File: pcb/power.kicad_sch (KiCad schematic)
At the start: 0 parts

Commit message: Completed Initial Power Draft for Review, and Updated Flags
Included notes for review
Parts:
- added C21: 1000pF, Capacitor_SMD:C_0402_1005Metric_Pad0.74x0.62mm_HandSolder, symbol Device:C_Small
- added C22: 0.47uF, Capacitor_SMD:C_0402_1005Metric_Pad0.74x0.62mm_HandSolder, symbol Device:C_Small
- added C23, C34: 1uF, Capacitor_SMD:C_0402_1005Metric_Pad0.74x0.62mm_HandSolder, symbol Device:C_Small
- added C24: 33uF, Capacitor_SMD:C_0402_1005Metric_Pad0.74x0.62mm_HandSolder, symbol Device:C_Small
- added C25: 3300pF, Capacitor_SMD:C_0402_1005Metric_Pad0.74x0.62mm_HandSolder, symbol Device:C_Small
- added C26, C28, C29, C31, C32: 0.1uF, Capacitor_SMD:C_0402_1005Metric_Pad0.74x0.62mm_HandSolder, symbol Device:C_Small
- added C27: 100uF, Capacitor_SMD:C_0402_1005Metric_Pad0.74x0.62mm_HandSolder, symbol Device:C_Small
- added C30, C33, C35, C36: 10uF, Capacitor_SMD:C_0402_1005Metric_Pad0.74x0.62mm_HandSolder, symbol Device:C_Small
- added D1: 5V, Diode_SMD:D_SOD-882, symbol Device:D_TVS_Small
- added L1: 15uH, symbol Device:L_Small
- added L2, L3: 8.2uH, symbol Device:L_Small
- added Q7: Vishay Si7465, symbol Simulation_SPICE:PMOS
- added R13: 0.01Ω, symbol Device:R_Small_US
- added R14: 2.1kΩ, symbol Device:R_Small_US
- added R15: 90.9kΩ, symbol Device:R_Small_US
- added R16: 66.5kΩ, symbol Device:R_Small_US
- added R17, R23: 10kΩ, symbol Device:R_Small_US
- added R18: 3.4kΩ, symbol Device:R_Small_US
- added R19, R21: 69.8kΩ, symbol Device:R_Small_US
- added R20, R22: 22.1kΩ, symbol Device:R_Small_US
- added U3: LM5085, symbol Symbols:LM5085
- added U4: LMR51610, symbol Symbols:LMR51610
- added U5: LMR51606, symbol Symbols:LMR51606
- added U6: LM2775, Package_SON:WSON-8-1EP_2x2mm_P0.5mm_EP0.9x1.6mm_ThermalVias, symbol Regulator_SwitchedCapacitor:LM2775DSG
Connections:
- new net: C25.2, C26.1, R16.2
- new net: C26.2, R17.2, R18.1, U3.3 (FB)
- new net: Q7.1 (D), R13.2, U3.5 (ISEN)
- new net: Q7.2 (G), U3.6 (PGATE)
- new net: D1.2 (A2), L1.1, Q7.3 (S), R16.1
- new net: R23.2, U6.5 (EN)
- new net: C32.1, U5.1 (CB)
- new net: C32.2, L3.1, U5.6 (SW)
- new net: C34.1, U6.3 (C1+)
- new net: C34.2, U6.2 (C1-)
- new net: C28.1, U4.1 (CB)
- new net: C28.2, L2.1, U4.6 (SW)
- new net: C21.2, R14.1, U3.1 (ADJ)
- new net: R15.2, U3.2 (RT)
- new net: R19.2, R20.1, U4.3 (FB)
- new net: R21.2, R22.1, U5.3 (FB)
- new net: C22.2, U3.7 (VCC)
- new net +3V3I: C33.1, L3.2, R21.1, R23.1
- new net +3V3P: C30.1, C36.1, L2.2, R19.1, U6.1 (PFM), U6.4 (OUTDIS), U6.7 (VIN)
- new net +5VCP: C35.1, U6.6 (VOUT)
- new net +5VP: C25.1, C27.1, L1.2, R17.1
- new net +VBAT: C21.1, C22.1, C23.1, C24.1, C29.1, C31.1, R13.1, R14.2, R15.1, U3.8 (VIN), U4.4 (EN), U4.5 (VIN), U5.4 (EN), U5.5 (VIN)
- new net GND: C23.2, C24.2, C27.2, C29.2, C30.2, C31.2, C33.2, C35.2, C36.2, D1.1 (A1), R18.2, R20.2, R22.2, U3.4 (GND), U4.2 (GND), U5.2 (GND), U6.8 (GND), U6.9 (GND)
- no-connect marks 0 -> 7
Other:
- note added: ""CHARGE PUMP""
- note added: "-"
- note added: "16V"
- note added: "3.3V Internal"
- note added: "3.3V Peripheral"
- note added: "5V Peripheral"
- note added: "Charge Pump"
- note added: "DOUBLE CHECK IF I CAN DO THIS"
- note added: "Daughter Board"
- note added: "Internal"
- note added: "Peripheral"
- note added: "Power Overview"
- note added: "Source"
- note added: "{dblquote}BATTERY{dblquote}"
- note added: "{dblquote}MOTOR{dblquote}"

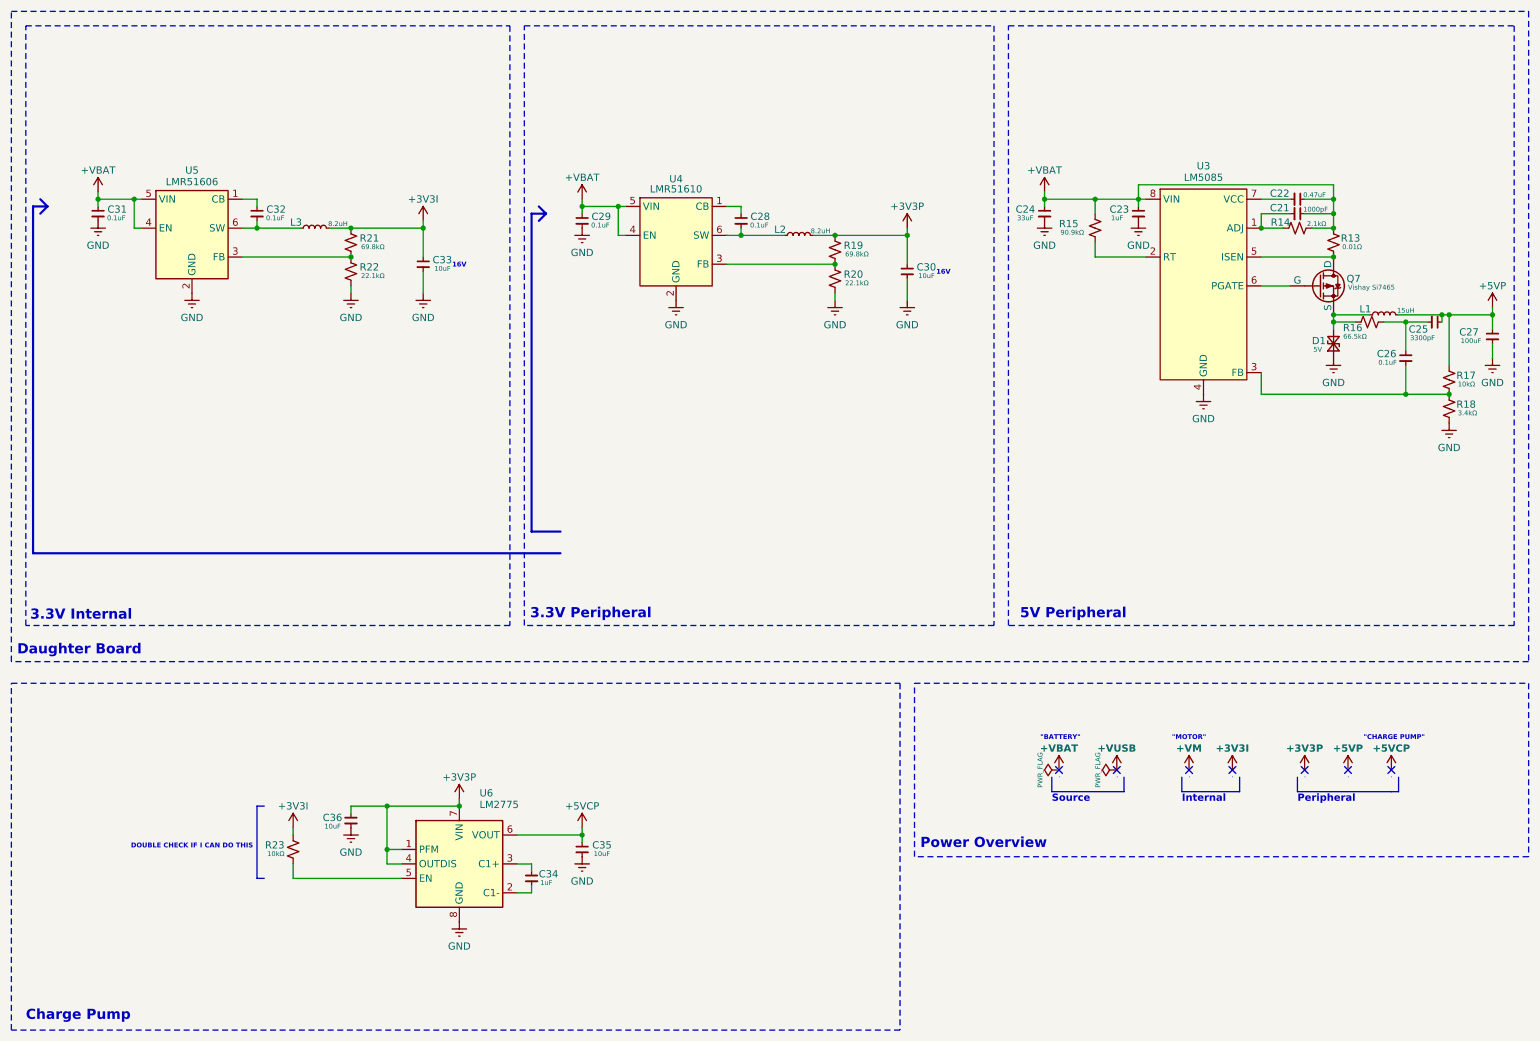
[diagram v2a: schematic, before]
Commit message: Made updates to the power and driver sheet
Fixed converters and added motor connector
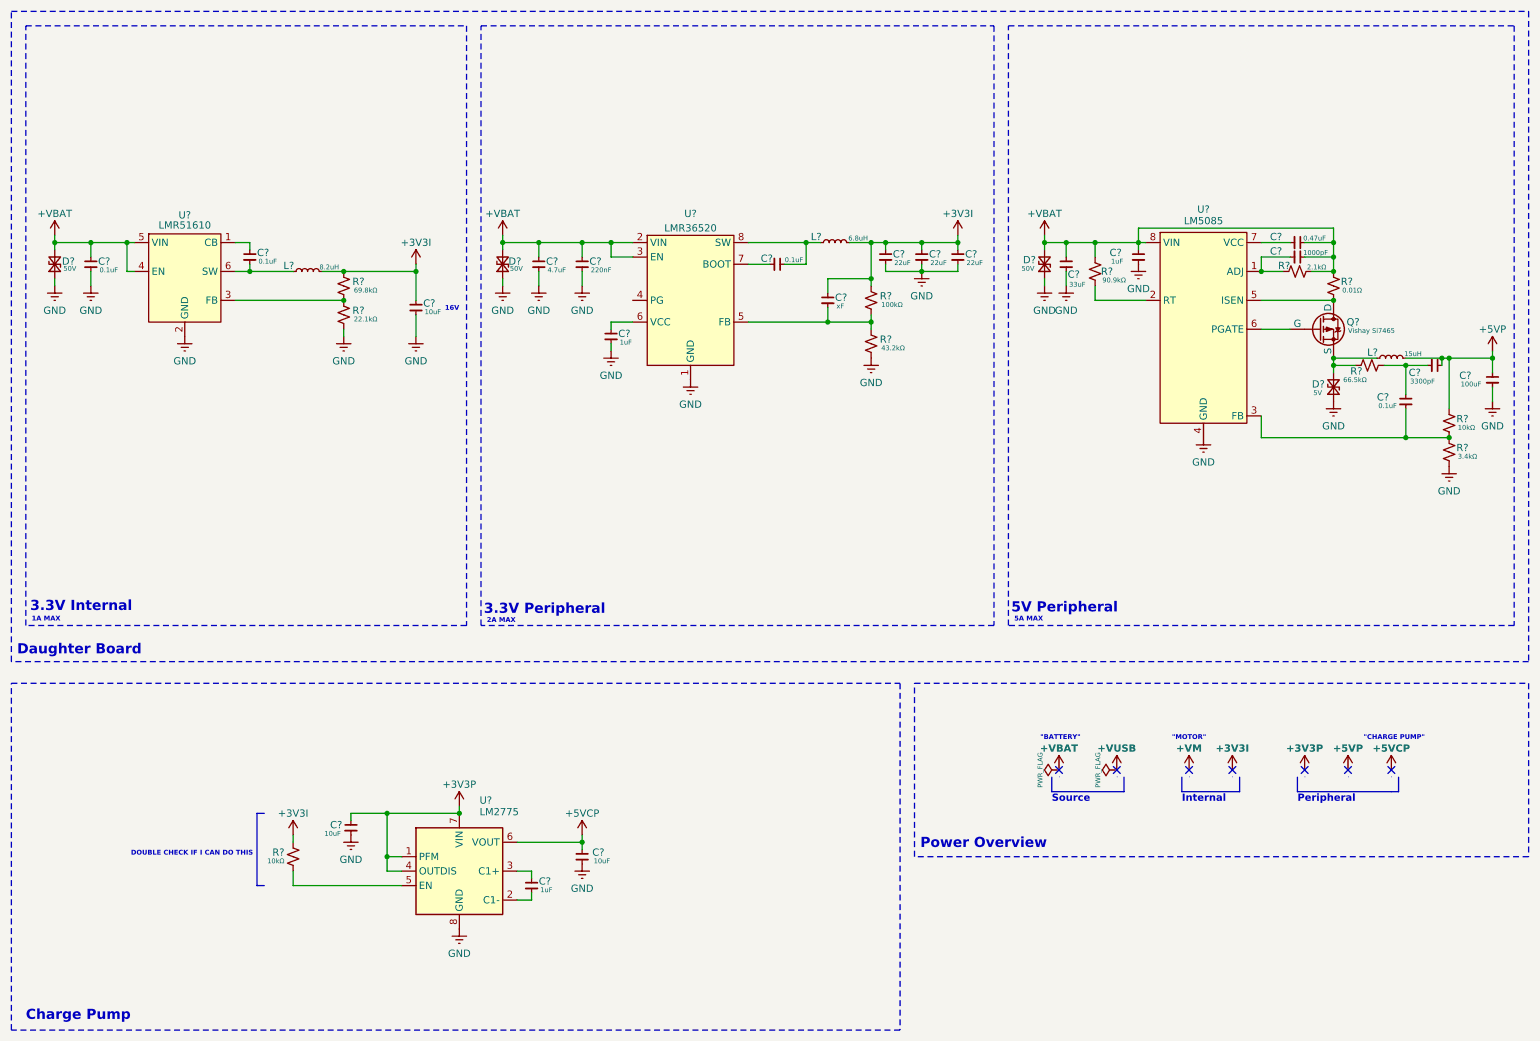
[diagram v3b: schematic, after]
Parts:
- removed C28, C29, C31, C32: 0.1uF, Capacitor_SMD:C_0402_1005Metric_Pad0.74x0.62mm_HandSolder, symbol Device:C_Small
- removed C30, C33: 10uF, Capacitor_SMD:C_0402_1005Metric_Pad0.74x0.62mm_HandSolder, symbol Device:C_Small
- removed L2, L3: 8.2uH, symbol Device:L_Small
- removed R19, R21: 69.8kΩ, symbol Device:R_Small_US
- removed R20, R22: 22.1kΩ, symbol Device:R_Small_US
- removed U4: LMR51610, symbol Symbols:LMR51610
- removed U5: LMR51606, symbol Symbols:LMR51606
- added C? (x3): 22uF, Capacitor_SMD:C_0402_1005Metric_Pad0.74x0.62mm_HandSolder, symbol Device:C_Small
- added C?: 220nF, Capacitor_SMD:C_0402_1005Metric_Pad0.74x0.62mm_HandSolder, symbol Device:C_Small
- added C?: xF, Capacitor_SMD:C_0402_1005Metric_Pad0.74x0.62mm_HandSolder, symbol Device:C_Small
- added C?: 4.7uF, Capacitor_SMD:C_0402_1005Metric_Pad0.74x0.62mm_HandSolder, symbol Device:C_Small
- added C? (x3): 0.1uF, Capacitor_SMD:C_0402_1005Metric_Pad0.74x0.62mm_HandSolder, symbol Device:C_Small
- added C?: 1uF, Capacitor_SMD:C_0402_1005Metric_Pad0.74x0.62mm_HandSolder, symbol Device:C_Small
- added C?: 10uF, Capacitor_SMD:C_0402_1005Metric_Pad0.74x0.62mm_HandSolder, symbol Device:C_Small
- added D? (x3): 50V, symbol Device:D_TVS_Small
- added L?: 8.2uH, symbol Device:L_Small
- added L?: 6.8uH, symbol Device:L_Small
- added R?: 69.8kΩ, symbol Device:R_Small_US
- added R?: 43.2kΩ, symbol Device:R_Small_US
- added R?: 100kΩ, symbol Device:R_Small_US
- added R?: 22.1kΩ, symbol Device:R_Small_US
- added U?: LMR51610, Package_TO_SOT_SMD:SOT-23-6_Handsoldering, symbol Symbols:LMR51610
- added U?: LMR36520, Package_SO:Texas_R-PDSO-G8_EP2.95x4.9mm_Mask2.4x3.1mm_ThermalVias, symbol Symbols:LMR36520
- renumbered C26 to C?, C34 to C?, C23 to C?, C21 to C?, C35 to C?, C25 to C?, C27 to C?, C22 to C?, C24 to C?, C36 to C?, D1 to D?, L1 to L?, Q7 to Q?, R23 to R?, R18 to R?, R16 to R?, R15 to R?, R17 to R?, R14 to R?, R13 to R?, U6 to U?, U3 to U?
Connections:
- net +3V3I: now also C?.1, C?.1, C?.1, C?.1, C?.1, L?.2, L?.2, R?.1, R?.1
- net +VBAT: now also C?.1, C?.1, C?.1, D?.2 (A2), D?.2 (A2), D?.2 (A2), U?.2 (VIN), U?.3 (EN), U?.4 (EN), U?.5 (VIN)
- net GND: now also C?.2, C?.2, C?.2, C?.2, C?.2, C?.2, C?.2, C?.2, D?.1 (A1), D?.1 (A1), D?.1 (A1), R?.2, R?.2, U?.1 (GND), U?.2 (GND), U?.9 (EP)
- new net: C?.2, L?.1, U?.6 (SW)
- new net: C?.1, U?.1 (CB)
- new net: R?.1, R?.2, U?.3 (FB)
- new net: C?.2, R?.1, R?.2, U?.5 (FB)
- new net: C?.1, U?.6 (VCC)
- new net: C?.2, U?.7 (BOOT)
- new net: C?.1, L?.1, U?.8 (SW)
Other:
- note added: "1A MAX"
- note added: "2A MAX"
- note added: "5A MAX"
- moved on the sheet: C?, D?, L?, Q?, R?, U?
